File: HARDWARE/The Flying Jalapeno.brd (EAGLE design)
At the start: 73.7 x 72.4 mm, 97 parts, among them Q1 BSS138, 200mA/50V, Q2 MMBT2222A, Q3 NDP6020P, Q4 MMBT2222A, Q5 NDP6020P, Q6 BSS138, 200mA/50V, U1 ATMEGA2560AU, U2 LM1117, U3 LM1117, U4 LM1117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

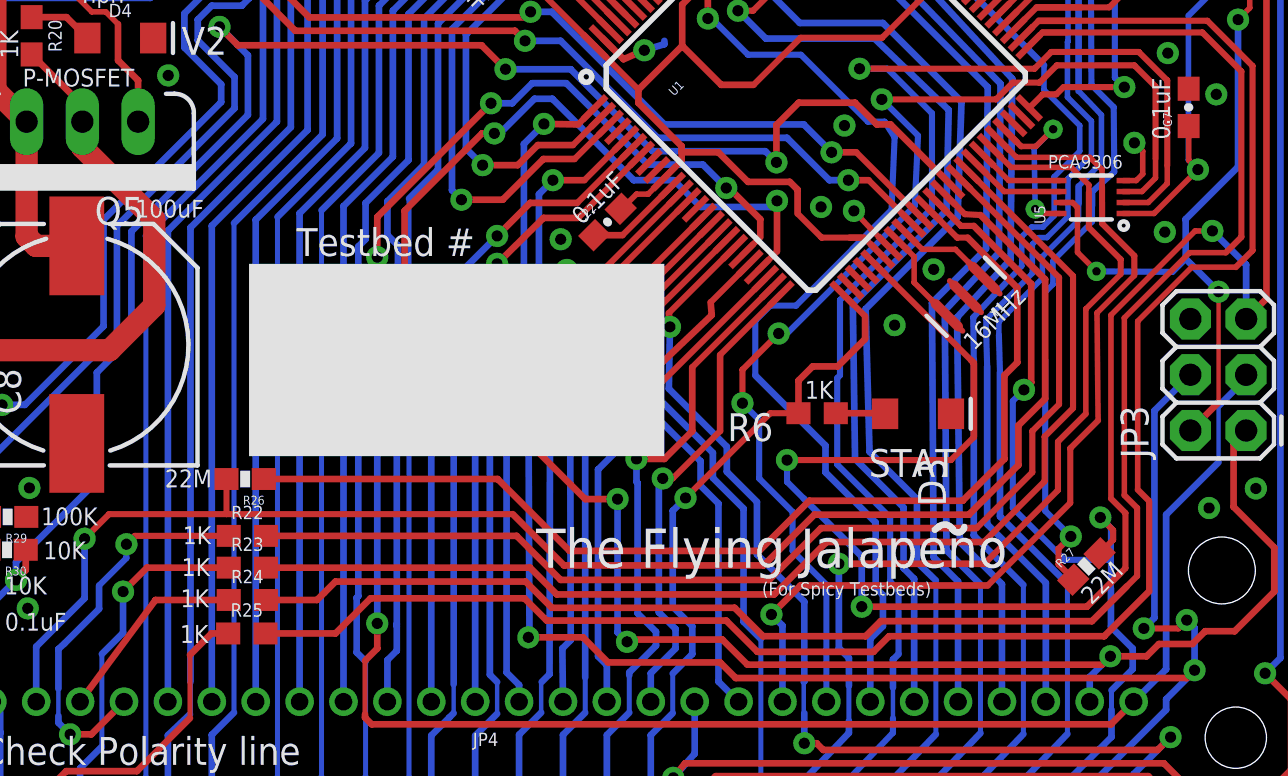
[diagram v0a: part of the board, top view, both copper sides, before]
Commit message: It begins
Removed PCA, joined capsense return lines (less complexity on board), swapped V2 line and RAW line to seperate V1 and V2. I also decreased the width to 20 mils (down from 40) on V1/2 according to trace width, length, and max current output. The suggested width courtesy Advanced Circuits trace calculator was 11 mil.  I removed LED resistors and renamed lines (thinking of using WS2812's according to Eric's initial design layout).
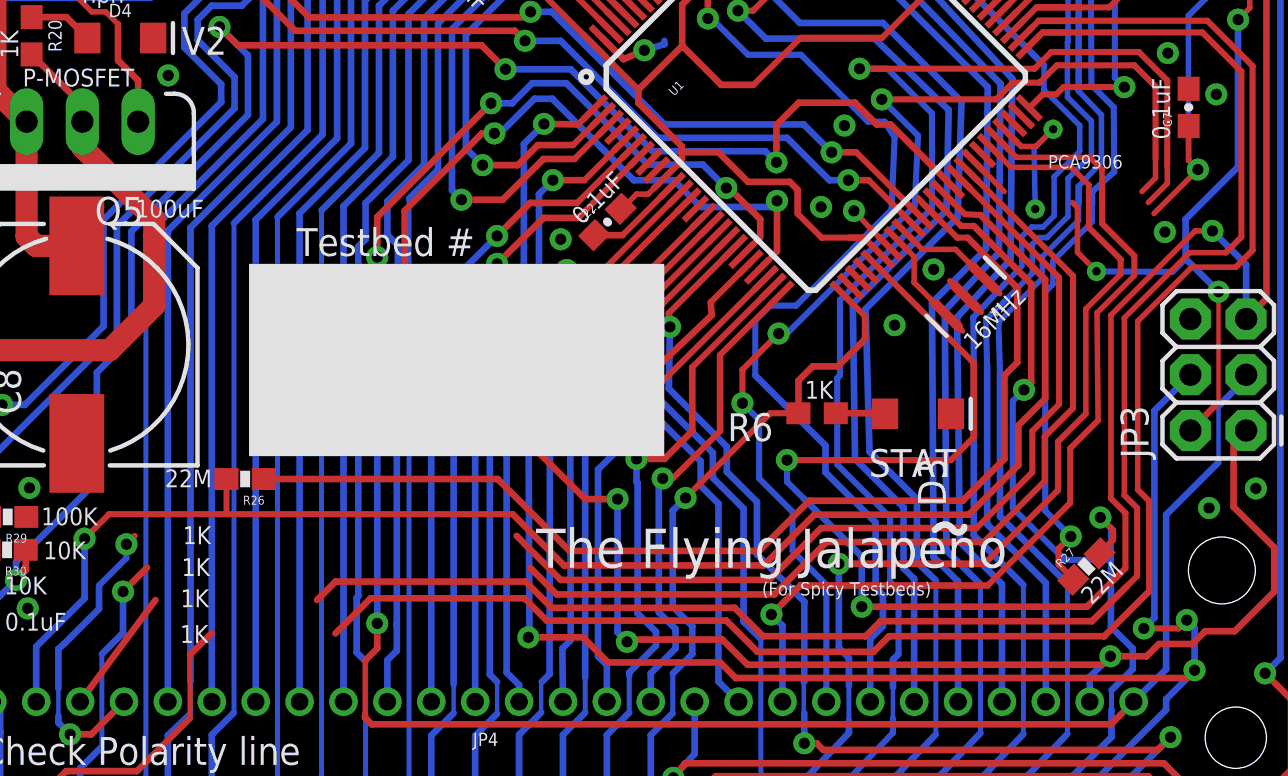
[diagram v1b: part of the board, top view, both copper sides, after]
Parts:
- removed R22, R23, R24, R25: 1k, SparkFun-Resistors:0603
- removed U5: PCA9306, SparkFun-DigitalIC:PCA9306DC-1:1
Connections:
- removed net 40/FAIL: R25.2, U1.52
- removed net 41/PASS: R24.2, U1.51
- removed net 42/PT_FAIL: R23.2, U1.42
- removed net 43/PT_PASS: R22.2, U1.41
- removed net N$19: JP4.6, R24.1
- removed net N$2: U1.44, U5.5
- removed net N$20: JP4.35, R25.1
- removed net N$27: U1.43, U5.6
- removed net N$6: JP4.7, R22.1
- removed net N$7: JP4.36, R23.1
- new net D40: JP4.35, U1.52
- new net D41: JP4.6, U1.51
- new net D42: JP4.36, U1.42
- new net D43: JP4.7, U1.41
- new net SCL: U1.43
- new net SDA: U1.44
- net 3.3V: no longer U5.1
- net EN_I2C: no longer U5.8
- net GND: no longer U5.4
- net SCL1: no longer U5.2
- net SDA1: no longer U5.3
- net VCC: no longer U5.7
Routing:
- net D40: track 0.00 -> 92.0 mm
- net D41: track 0.00 -> 82.7 mm
- net 40/FAIL: track 82.3 -> 0.00 mm
- net 41/PASS: track 79.3 -> 0.00 mm
- net D43: track 0.00 -> 56.0 mm, vias 0 -> 2
- net 42/PT_FAIL: track 54.8 -> 0.00 mm
- net D42: track 0.00 -> 54.8 mm, vias 0 -> 1
- net 43/PT_PASS: track 53.6 -> 0.00 mm
- net N$6: track 18.1 -> 0.00 mm, vias 2 -> 0
- net N$7: track 15.7 -> 0.00 mm, vias 1 -> 0
- net N$20: track 13.7 -> 0.00 mm
- net N$19: track 9.10 -> 0.00 mm
- net N$27: track 4.43 -> 0.00 mm
- net N$2: track 4.02 -> 0.00 mm
- net GND: track 24.5 -> 21.9 mm, vias 23 -> 22
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
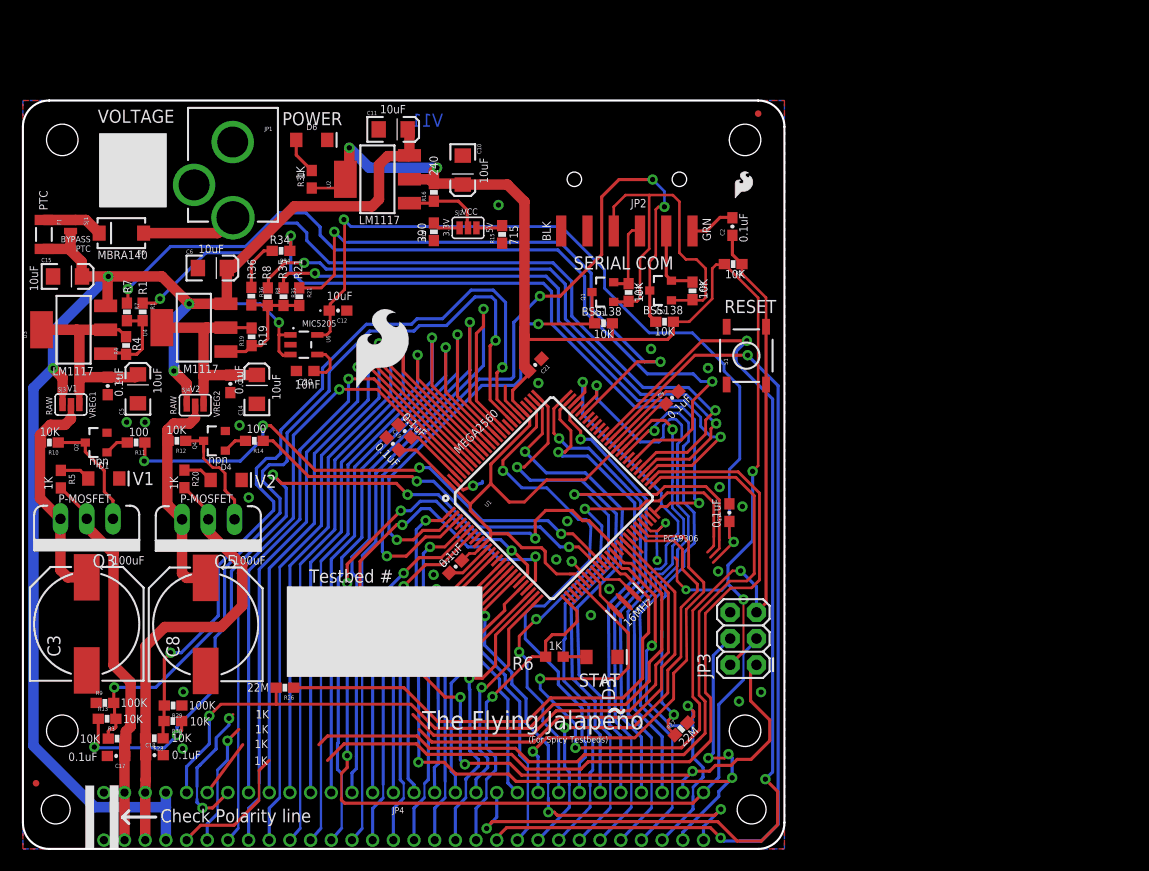
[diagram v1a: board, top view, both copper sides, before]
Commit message: Removed regulator, started rerouting
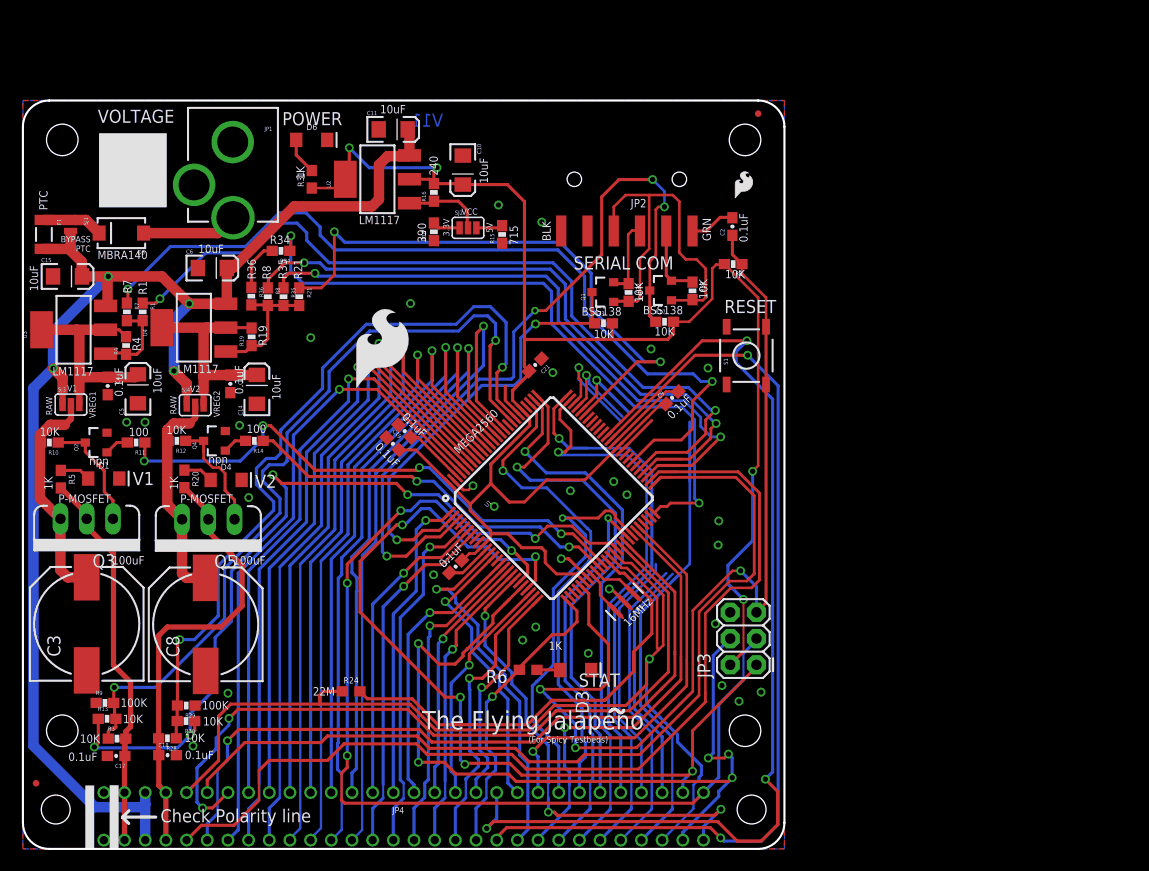
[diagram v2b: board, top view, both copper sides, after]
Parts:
- removed C12: 10uF, SparkFun-Capacitors:0603-POL
- removed C20: 10nF, SparkFun-Capacitors:0603
- removed C7: 0.1uF, SparkFun-Capacitors:0603-CAP
- removed R26, R27: 22M, SparkFun-Resistors:0603-RES
- removed U6: 3.3V MIC5205, SparkFun-PowerIC:SOT23-5
- added R24: 22M, SparkFun-Resistors:0603
- moved D3 2.84 mm to (53.5, 17.3)
- moved R6 2.84 mm to (48.9, 17.3)
- moved R30 1.27 mm to (15.8, 12.4)
- moved C18 1.27 mm to (14.0, 9.07)
- moved R28 1.27 mm to (14.0, 10.7)
- moved R29 1.27 mm to (15.8, 13.9)
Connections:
- removed net 3.3V: C12.A, C7.1, U6.5
- removed net 31/CAPRETURN2: R27.1, U1.59
- removed net 45/CAPSENSE1: JP4.5, R26.2, U1.39
- removed net 46/CAPSENSE2: JP4.58, R27.2, U1.38
- removed net 47/CAPRETURN1: R26.1, U1.37
- removed net EN_I2C: U1.47
- removed net N$28: C20.1, U6.4
- removed net SCL1: JP4.53
- removed net SDA1: JP4.23
- new net 45_46/CAPSENSE: JP4.5, JP4.58, R24.1, U1.38, U1.39
- new net CAPRETURN: R24.2, U1.37
- net GND: no longer C12.K, C20.2, C7.2, U6.2
- net RAW: now also JP4.3, JP4.33; no longer JP4.34, JP4.4, U6.1, U6.3
- net SCL: now also JP4.53
- net SDA: now also JP4.23
- net V2: now also JP4.34, JP4.4; no longer JP4.3, JP4.33
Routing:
- net 45_46/CAPSENSE: track 0.00 -> 105.0 mm, vias 0 -> 1
- net 3.3V: track 79.9 -> 0.00 mm, vias 2 -> 0
- net 45/CAPSENSE1: track 71.0 -> 0.00 mm, vias 1 -> 0
- net SCL1: track 60.6 -> 0.00 mm, vias 1 -> 0
- net SDA1: track 51.7 -> 0.00 mm, vias 3 -> 0
- net 47/CAPRETURN1: track 50.4 -> 0.00 mm
- net CAPRETURN: track 0.00 -> 43.5 mm
- net 31/CAPRETURN2: track 42.3 -> 0.00 mm, vias 2 -> 0
- net 46/CAPSENSE2: track 39.3 -> 0.00 mm, vias 2 -> 0
- net SDA: track 0.00 -> 39.2 mm, vias 0 -> 1
- net SCL: track 1.89 -> 38.2 mm, vias 0 -> 1
- net D43: track 56.0 -> 74.0 mm
- net D42: track 54.8 -> 72.2 mm
- net D30: track 45.5 -> 28.3 mm, vias 1 -> 0
- net RAW: track 153.3 -> 136.7 mm, vias 5 -> 4
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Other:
- board text added: "Revised by: Elias Santistevan"
- board text removed: "10nF"
- board text removed: "MIC5205"
- board text removed: "PCA9306"
- board text removed: "Testbed #"

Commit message: smaller caps, capsense, ws2812's
Smaller capacitors 10uf down from 100uf, added to lines preceding high side switch. I'll be rerouting Atmega to make sense of where the ws2812's and capsense will sit but wanted to sync before I do that.
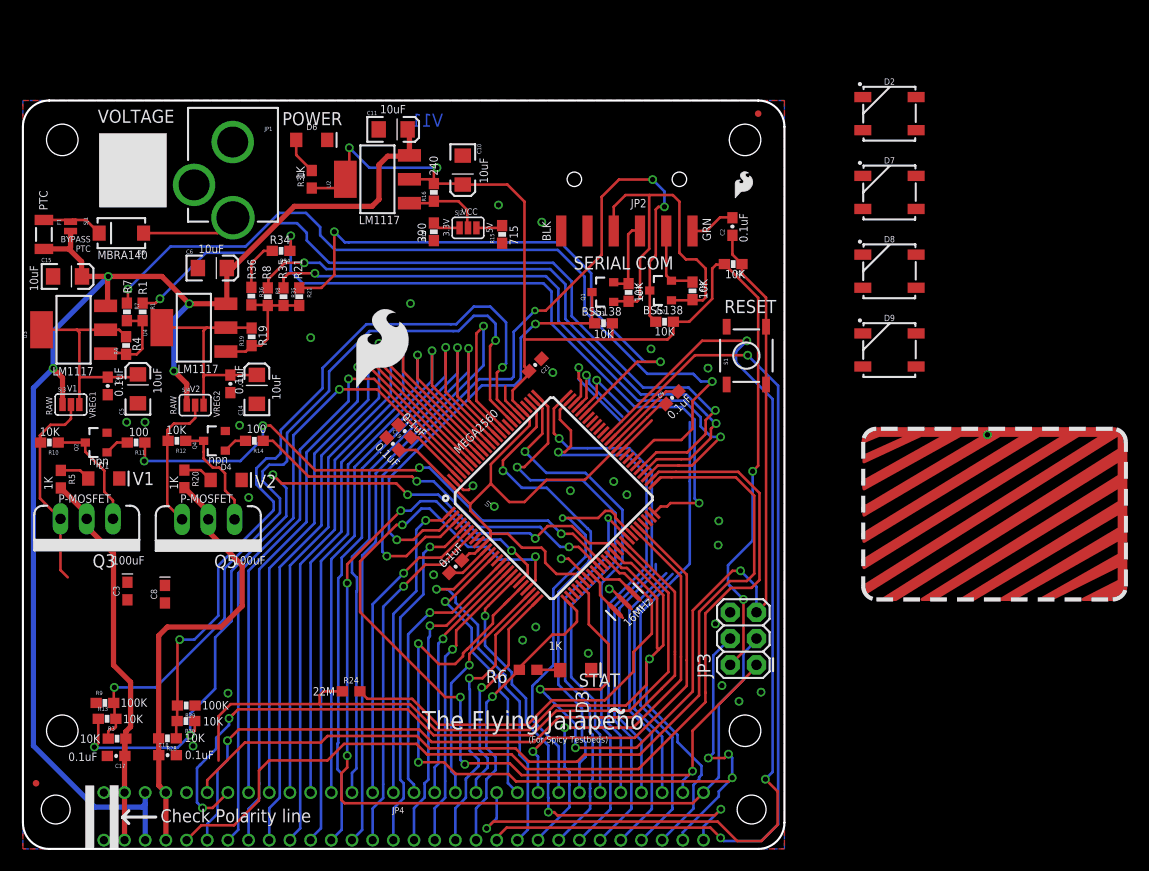
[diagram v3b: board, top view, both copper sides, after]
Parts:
- added D2, D7, D8, D9: WS2812B, SparkFun-LED:WS2812B
- added U$1: CAPSENSE_BUTTON_PAD_ONLY, Testing:CAPSENSE_BUTTON_PADS_ONLY
- C10, C11, C14, C15, C5, C6: device SparkFun-Capacitors:EIA3216 -> SparkFun-Capacitors:EIA3216@1
- C3, C8: value 100uF -> 10uF; device SparkFun-Capacitors:NIC_10X10.5_CAP -> SparkFun-Capacitors:0603-POLAR
- moved C3 5.06 mm to (10.1, 24.9)
- moved C8 4.90 mm to (13.7, 24.6)
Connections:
- net 45_46/CAPSENSE: now also U$1.CAPSENSE_PAD; no longer JP4.5, JP4.58
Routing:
- net N$23: track 22.5 -> 14.8 mm
- net 45_46/CAPSENSE: track 105.0 -> 100.6 mm
- net N$22: track 22.4 -> 20.6 mm

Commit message: Header moved to right side
Making some space for programming adapter.
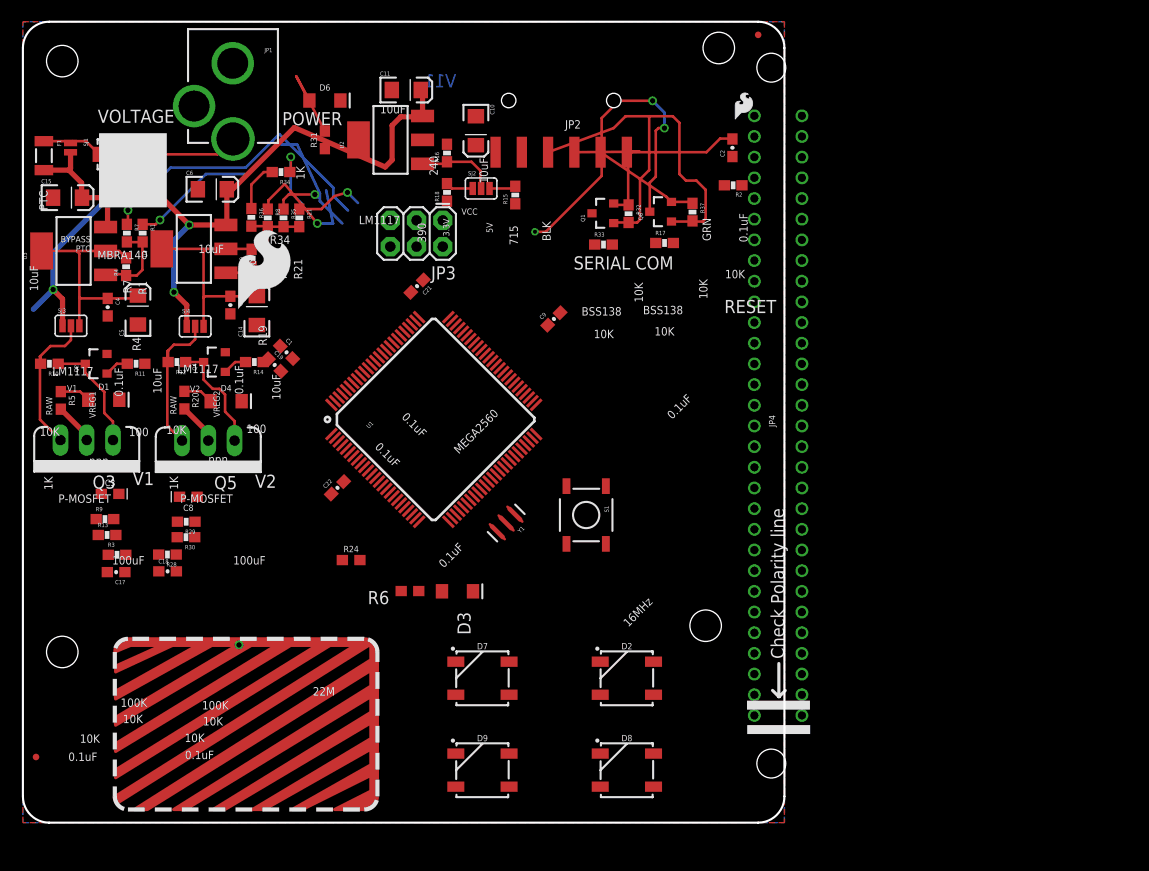
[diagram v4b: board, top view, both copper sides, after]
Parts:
- moved U$1 75.2 mm to (21.6, 12.7)
- moved D7 61.3 mm to (44.5, 16.5)
- moved D2 60.2 mm to (58.4, 16.5)
- moved JP4 57.5 mm to (76.2, 41.9), turned to 90 degrees
- moved D9 56.6 mm to (44.5, 7.62)
- moved D8 54.5 mm to (58.4, 7.62)
- moved JP3 52.6 mm to (40.6, 60.8), turned to 180 degrees
- moved S1 21.9 mm to (54.5, 32.3), turned to 270 degrees
- moved C17 17.8 mm to (9.02, 26.8)
- moved C18 17.8 mm to (14.0, 26.8)
- moved R13 17.8 mm to (8.14, 30.4)
- moved R28 17.8 mm to (14.0, 28.5)
- moved R29 17.8 mm to (15.8, 31.6)
- moved R3 17.8 mm to (9.11, 28.4)
- moved R30 17.8 mm to (15.8, 30.1)
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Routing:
- net VCC: track 182.2 -> 0.00 mm, vias 4 -> 0
- net 45_46/CAPSENSE: track 100.6 -> 0.00 mm, vias 1 -> 0
- net TX3: track 100.6 -> 0.00 mm, vias 3 -> 0
- net PB1: track 100.2 -> 0.00 mm, vias 4 -> 0
- net RESET: track 94.9 -> 0.00 mm, vias 3 -> 0
- net D40: track 94.7 -> 0.00 mm
- net RX3: track 92.3 -> 0.00 mm, vias 2 -> 0
- net PB3: track 87.5 -> 0.00 mm, vias 5 -> 0
- net D41: track 87.4 -> 0.00 mm
- net PB2: track 83.0 -> 0.00 mm, vias 5 -> 0
- net 44/PT_CTRL: track 81.5 -> 0.00 mm, vias 5 -> 0
- net A14/PT_READ_V1: track 78.5 -> 0.00 mm, vias 2 -> 0
- net A15/PT_READ_V2: track 75.6 -> 0.00 mm, vias 2 -> 0
- net D43: track 74.0 -> 0.00 mm, vias 2 -> 0
- net D42: track 72.2 -> 0.00 mm, vias 1 -> 0
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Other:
- board size 73.7 x 72.4 mm -> 73.7 x 77.5 mm
- board text removed: "(For Spicy Testbeds)"
- board text removed: "STAT"
- board text removed: "The Flying Jalapeno"
